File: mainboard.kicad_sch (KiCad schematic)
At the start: 95 parts, among them J1 Conn 02x05 1.27mm, J10 Micro_SD_Card, J2 TFM-110-12-L-D-A, J3 SFC-110-T2-F-D-A, J4 CLP-105-02-X-DH-A, J5 CLP-105-02-X-DH-A, J6 CLP-105-02-X-DH-A, J7 CLP-105-02-X-DH-A, J8 U.FL-R-SMT-1, J9 USB_C_Receptacle_USB2.0, SW1 KMR231NG, SW2 SW_SPDT, U1 ATSAMD51J20A-M, U10 USBLC6-2SC6, U11 PCF8523TK, U2 MAX706RESA+, U3 AP2112K-3.3, U4 MR25H40, U5 BMX160, U6 RFM98PW, U7 DRV8830DRC, U8 DRV8830DRC, U9 DRV8830DRC, Y1 32.768kHz, Y2 32.768kHz

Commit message: Added Pullup to SD CS
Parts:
- added R69: 10K, Resistor_SMD:R_0603_1608Metric, symbol Device:R_US
- R92, R93: symbol Device:R_Small -> Device:R_US
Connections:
- net +3V3: now also R69.1
- net SD_CS: now also R69.2
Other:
- note added: "I2C1 ADDR"
- note added: "I2C2 ADDR"
- note added: "X BOARD COILS I2C1 ADDR 0x60"
- note added: "Y BOARD COILS I2C1 ADDR 0x62"
- note added: "Z BOARD COILS I2C1 ADDR 0x68"
- note removed: "I2C ADDR"
- moved on the sheet: J4, J5, J6, J7, R26, R27, R28

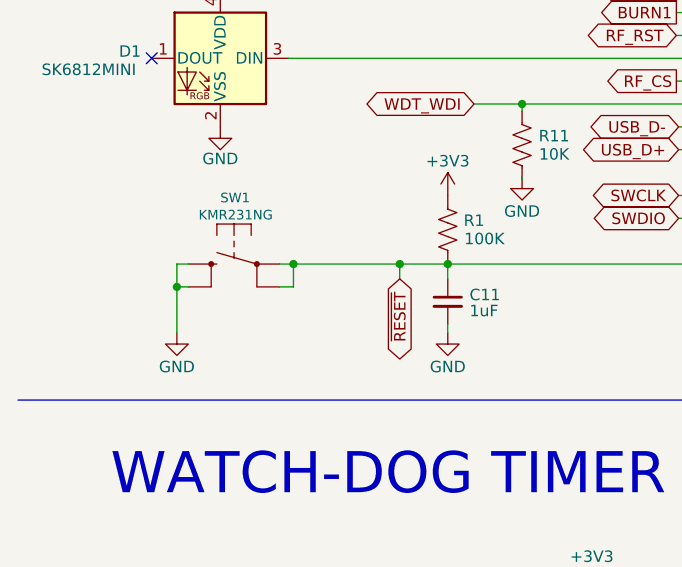
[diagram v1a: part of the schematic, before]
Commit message: right-angle reset button + export STEP / BOM
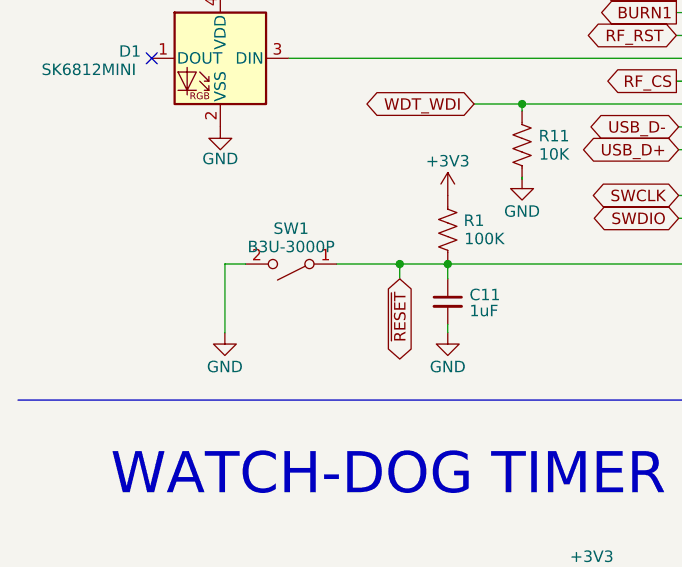
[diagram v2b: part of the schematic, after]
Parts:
- removed SW1: KMR231NG, mainboard:BTN_KMR2_4.6X2.8, symbol mainboard:SWITCH_TACT_SMT4.6X2.8-
- added SW1: B3U-3000P, Button_Switch_SMD:SW_SPST_B3U-3000P, symbol Switch:SW_SPST
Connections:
- net GND: now also SW1.2 (B)
- net ~{RESET}: now also SW1.1 (A)
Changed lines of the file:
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@@
   (junction (at 142.24 34.036) (diameter 0) (color 0 0 0 0)
   )
-  (junction (at 29.591 131.445) (diameter 0) (color 0 0 0 0)
-  )
   (junction (at 165.354 90.805) (diameter 0) (color 0 0 0 0)
   )
@@
   (junction (at 142.24 39.116) (diameter 0) (color 0 0 0 0)
   )
-  (junction (at 42.545 128.905) (diameter 0) (color 0 0 0 0)
-  )
   (junction (at 187.071 163.703) (diameter 0) (color 0 0 0 0)
   )
@@
     (stroke (width 0) (type default) (color 0 0 0 0))
   )
-  (wire (pts (xy 29.591 131.445) (xy 30.861 131.445))
-    (stroke (width 0) (type default) (color 0 0 0 0))
-  )
   (wire (pts (xy 386.588 189.357) (xy 393.065 189.357))
     (stroke (width 0) (type default) (color 0 0 0 0))
@@
     (stroke (width 0) (type default) (color 0 0 0 0))
   )
-  (wire (pts (xy 41.021 131.445) (xy 42.545 131.445))
-    (stroke (width 0) (type default) (color 0 0 0 0))
-  )
   (wire (pts (xy 182.372 38.1) (xy 178.816 38.1))
     (stroke (width 0) (type default) (color 0 0 0 0))
@@
     (stroke (width 0) (type default) (color 0 0 0 0))
   )
-  (wire (pts (xy 29.591 128.905) (xy 29.591 131.445))
-    (stroke (width 0) (type default) (color 0 0 0 0))
-  )
   (wire (pts (xy 142.367 83.185) (xy 142.367 85.725))
     (stroke (width 0) (type default) (color 0 0 0 0))
@@
     (stroke (width 0) (type default) (color 0 0 0 0))
   )
-  (wire (pts (xy 42.545 128.905) (xy 54.356 128.905))
+  (wire (pts (xy 47.371 128.905) (xy 54.356 128.905))
     (stroke (width 0) (type default) (color 0 0 0 0))
   )
@@
     (stroke (width 0) (type solid) (color 0 0 0 0))
   )
-  (wire (pts (xy 41.021 128.905) (xy 42.545 128.905))
-    (stroke (width 0) (type default) (color 0 0 0 0))
-  )
   (wire (pts (xy 342.138 213.741) (xy 343.789 213.741))
     (stroke (width 0) (type default) (color 0 0 0 0))
@@
     (stroke (width 0) (type default) (color 0 0 0 0))
   )
-  (wire (pts (xy 29.591 128.905) (xy 30.861 128.905))
+  (wire (pts (xy 34.925 128.905) (xy 37.211 128.905))
     (stroke (width 0) (type default) (color 0 0 0 0))
   )
@@
     (stroke (width 0) (type solid) (color 0 0 0 0))
   )
-  (wire (pts (xy 42.545 131.445) (xy 42.545 128.905))
-    (stroke (width 0) (type default) (color 0 0 0 0))
-  )
   (wire (pts (xy 247.142 145.542) (xy 247.142 148.082))
     (stroke (width 0) (type default) (color 0 0 0 0))
@@
     (stroke (width 0) (type default) (color 0 0 0 0))
   )
-  (wire (pts (xy 29.591 131.445) (xy 29.591 136.525))
+  (wire (pts (xy 34.925 128.905) (xy 34.925 136.525))
     (stroke (width 0) (type default) (color 0 0 0 0))
   )
@@
     )
   )
-  (symbol (lib_id "mainboard:SWITCH_TACT_SMT4.6X2.8-") (at 35.941 128.905 0) (mirror y) (unit 1)
-    (in_bom yes) (on_board yes)
-    (property "Reference" "SW1" (id 0) (at 37.719 122.174 0)
-      (effects (font (size 1.0668 1.0668)) (justify left bottom))
-    )
-    (property "Value" "KMR231NG" (id 1) (at 40.259 124.079 0)
-      (effects (font (size 1.0668 1.0668)) (justify left bottom))
-    )
-    (property "Footprint" "mainboard:BTN_KMR2_4.6X2.8" (id 2) (at 35.941 128.905 0)
-      (effects (font (size 1.27 1.27)) hide)
-    )
-    (property "Datasheet" "https://www.ckswitches.com/media/1479/kmr2.pdf" (id 3) (at 35.941 128.905 0)
-      (effects (font (size 1.27 1.27)) hide)
-    )
-    (pin "A")
-    (pin "A'")
-    (pin "B")
-    (pin "B'")
-  )
   (symbol (lib_id "Device:R_US") (at 59.69 125.095 180) (unit 1)
     (in_bom yes) (on_board yes)
@@
     (pin "1")
   )
-  (symbol (lib_id "power:GND") (at 29.591 136.525 0) (unit 1)
+  (symbol (lib_id "power:GND") (at 34.925 136.525 0) (unit 1)
     (in_bom yes) (on_board yes)
-    (property "Reference" "#PWR02" (id 0) (at 29.591 142.875 0)
+    (property "Reference" "#PWR02" (id 0) (at 34.925 142.875 0)
       (effects (font (size 1.27 1.27)) hide)
     )
-    (property "Value" "GND" (id 1) (at 29.591 140.335 0))
-    (property "Footprint" "" (id 2) (at 29.591 136.525 0)
+    (property "Value" "GND" (id 1) (at 34.925 140.335 0))
+    (property "Footprint" "" (id 2) (at 34.925 136.525 0)
       (effects (font (size 1.27 1.27)) hide)
     )
-    (property "Datasheet" "" (id 3) (at 29.591 136.525 0)
+    (property "Datasheet" "" (id 3) (at 34.925 136.525 0)
       (effects (font (size 1.27 1.27)) hide)
     )
@@
     (pin "1")
   )
+  (symbol (lib_id "Switch:SW_SPST") (at 42.291 128.905 180) (unit 1)
+    (in_bom yes) (on_board yes)
+    (property "Reference" "SW1" (id 0) (at 42.291 124.968 0))
+    (property "Value" "B3U-3000P" (id 1) (at 42.291 127 0))
+    (property "Footprint" "Button_Switch_SMD:SW_SPST_B3U-3000P" (id 2) (at 42.291 128.905 0)
+      (effects (font (size 1.27 1.27)) hide)
+    )
+    (property "Datasheet" "~" (id 3) (at 42.291 128.905 0)
+      (effects (font (size 1.27 1.27)) hide)
+    )
+    (pin "1")
+    (pin "2")
+  )
   (symbol (lib_id "Device:R_US") (at 359.283 38.735 90) (unit 1)
     (in_bom yes) (on_board yes)
@@
       (reference "R106") (unit 1) (value "10K") (footprint "Resistor_SMD:R_0603_1608Metric")
     )
-    (path "/00000000-0000-0000-0000-00005c6b86a4"
-      (reference "SW1") (unit 1) (value "KMR231NG") (footprint "mainboard:BTN_KMR2_4.6X2.8")
+    (path "/ace5ed3d-6dc5-4eeb-9b9e-b9cae91d4881"
+      (reference "SW1") (unit 1) (value "B3U-3000P") (footprint "Button_Switch_SMD:SW_SPST_B3U-3000P")
     )
     (path "/b6f24720-0eec-4e84-ad7b-6ef73d6ff170"

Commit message: Cleanup
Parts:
- C6: renamed from C7; value 10pF -> 4pF
- C7: renamed from C6; value 10pF -> 4pF
- D1: value SK6812MINI -> SK6812-MINI; footprint mainboard:NeoPixel 3535 -> LED_SMD:LED_SK6812MINI_PLCC4_3.5x3.5mm_P1.75mm
- J2: renamed from J8; symbol mainboard:U.FL-R-SMT-1-symbols -> mainboard:U.FL-R-SMT-1
- J5: renamed from J3; value SFC-110-T2-F-D-A -> SFC-110-T2-X-D-A
- J6: renamed from J2; value TFM-110-12-L-D-A -> TFM-110-12-X-D-A
- U1: value ATSAMD51J20A-M -> ATSAMD51J19A-M; symbol mainboard:ATSAMD51J20A-M-MCU_Microchip_SAMD -> mainboard:ATSAMD51J19A-M
- U2: symbol mainboard:MAX708RESA-T-symbols -> mainboard:MAX708RESA-T
- U5: symbol mainboard:BMX160-symbols -> mainboard:BMX160
- U6: symbol mainboard:RFM98PW-symbols -> mainboard:RFM98PW
- U7, U8, U9: symbol mainboard:DRV8830DRC-wbraun_ic_lib -> mainboard:DRV8830DRC
- renumbered C34 to C12, C12 to C13, C13 to C14, C14 to C15, C15 to C16, C32 to C17, C33 to C18, C16 to C19, C18 to C20, C19 to C21, C35 to C22, C20 to C23, C21 to C24, C22 to C25, C23 to C26, C17 to C27, J7 to J10, J10 to J3, J9 to J4, J4 to J7, J5 to J8, J6 to J9, R3 to R1, R11 to R10, R1 to R11, R22 to R12, R12 to R13, R13 to R14, R80 to R15, R14 to R16, R15 to R17, R16 to R18, R69 to R19, R4 to R2, R18 to R20, R19 to R21, R20 to R22, R17 to R26, R70 to R27, R93 to R28, R92 to R29, R9 to R3, R26 to R30, R27 to R31, R28 to R32, R10 to R4, R21 to R9
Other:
- note added: "Check Xtal Datasheet This value assumes 7pF crystal bulk capacitance"
- note added: "RTC supports 7pF (default) and 12.5pF crystal capacitance only"
- moved on the sheet: C13, C19

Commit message: Stash before major changes
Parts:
- removed SW1: B3U-3000P, Button_Switch_SMD:SW_SPST_B3U-3000P, symbol Switch:SW_SPST
- added Q23: IRLML2803, Package_TO_SOT_SMD:SOT-23, symbol Transistor_FET:IRLML2060
- added R103: DNI (0R), Resistor_SMD:R_0603_1608Metric, symbol Device:R_US
- added R104: 200K, Resistor_SMD:R_0603_1608Metric, symbol Device:R_US
- added SW1: KMS233, mainboard:BTN_KMS2, symbol mainboard:BTN_KMS2
- D1: footprint LED_SMD:LED_SK6812MINI_PLCC4_3.5x3.5mm_P1.75mm -> mainboard:SK6812-MINI
- J3: footprint mainboard:microSD_HC_Molex_104031-0811 -> mainboard:microSD_104031-0811; symbol Connector:Micro_SD_Card_Det -> Connector:Micro_SD_Card_Det2
- J5: footprint mainboard:SAMTEC_SFC-110-T2-F-D-A-TR -> mainboard:SAMTEC_SFC-110-T2-X-D-A
- J6: footprint mainboard:SAMTEC_TFM-110-12-L-D-A -> mainboard:SAMTEC_TFM-110-12-X-D-A
- R20, R21, R22, R26, R30, R31, R32: value 0 -> 0R
- R28, R29: value 22 -> 22R
- SW2: value SW_SPDT -> PCM12SMTR; footprint mainboard:SW_PCM12SMTR -> mainboard:PCM12SMTR
- U2: symbol mainboard:MAX708RESA-T -> mainboard:MAX708RESA+
- U4: footprint mainboard:SON127P600X500X90-9N -> mainboard:MR25H40DF
- U6: footprint mainboard:RFM95PW -> mainboard:RFM98PW
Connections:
- net GND: now also R104.2, SW1.1 (S), SW1.2 (S1), SW1.5
- net ~{RESET}: now also Q23.3 (D), R103.1, SW1.3 (P), SW1.4 (P1); no longer R13.1
- net WDT_EN: now reaches U1.49 (PB22)
- net WDT_EN: now also Q23.1 (G), R104.1
- new net: Q23.2 (S), R103.2, R13.1
- no-connect marks 35 -> 34
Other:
- note added: "WDT able to reset MCU when WDT_EN is high"
- note removed: "WDT enabled when installed"
- moved on the sheet: C13, R11, R13, U2

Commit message: Finished routing Rev B3/01
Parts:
- removed D1: SK6812-MINI, mainboard:SK6812-MINI, symbol LED:SK6812MINI
- removed FID1, FID2, FID3: Fiducial, Fiducial:Fiducial_0.5mm_Mask1mm, symbol Mechanical:Fiducial
- removed SW2: PCM12SMTR, mainboard:PCM12SMTR, symbol Switch:SW_SPDT
- removed U5: BMX160, mainboard:BMX160, symbol mainboard:BMX160
- added C36: 0.1uF, Capacitor_SMD:C_0603_1608Metric, symbol Device:C_Small
- added C37, C38: 22pF, Capacitor_SMD:C_0603_1608Metric, symbol Device:C_Small
- added D1: SK6812-SIDE, mainboard:SK6812-SIDE, symbol mainboard:SK6812-SIDE
- added D2: MBR1020VL-AU_R1, Diode_SMD:D_SOD-123F, symbol Device:D_Schottky_Small
- added Q20: SQ3495EV-T1, Package_TO_SOT_SMD:SOT-23-6, symbol cameraboard:SQ3495EV-T1
- added R81, R82, R83: 10K, Resistor_SMD:R_0603_1608Metric, symbol Device:R_US
- added U12: BNO085, mainboard:BNO085, symbol mainboard:BNO085
- added U5: LTC4412xS6, Package_TO_SOT_SMD:TSOT-23-6, symbol Power_Management:LTC4412xS6
- added Y3: 32.768kHz, Crystal:Crystal_SMD_MicroCrystal_CC7V-T1A-2Pin_3.2x1.5mm, symbol Device:Crystal_Small
- C20: value 0.1uF -> 1uF
- renumbered Q23 to Q21, R104 to R100, R103 to R99
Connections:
- net +3V3: now also R18.2, D1.2 (VDD), R81.2, R82.1, U12.28 (VDDIO), U12.3 (VDD), U12.5 (PS1), U12.6 (PS0/WAKE); no longer C20.1, R18.1
- net BATT_P: now also C20.1, Q20.1 (D), Q20.2 (D), Q20.5 (D), Q20.6 (D), U5.1 (VIN)
- net GND: now also C36.2, C37.1, C38.2, D1.4 (VSS), R83.1, U12.10 (CLKSEL0), U12.2 (GND), U12.25 (GNDIO), U5.2 (GND), U5.3 (CTL)
- net HI_POW: now also D2.1 (K), Q20.4 (S), U5.6 (SENSE); no longer U8.7 (A0), U8.8 (A1), U9.7 (A0)
- net VUSB_IN: now also D2.2 (A)
- net IMU_CS: now reaches U1.32 (PA15)
- net IMU_CS: now also R82.2, U12.18 (H_CSN)
- net at U1.42 (PA21): now also D1.1 (DIN)
- new net: C37.2, U12.27 (XIN32), Y3.1
- new net: C38.1, U12.26 (CLKSEL1/XOUT32), Y3.2
- new net: C36.1, U12.9 (CAP)
- new net: Q20.3 (G), U5.5 (GATE)
- new net: R81.1, U12.11 (NRST)
- new net: R18.1, U12.4 (BOOTN)
- new net: U12.1 (NC), U12.12 (NC), U12.13 (NC), U12.21 (NC), U12.22 (NC), U12.23 (NC), U12.24 (NC), U12.7 (NC), U12.8 (NC)
- new net ADPT_STAT: U5.4 (STAT)
- new net IMU_MISO: U12.20 (H_SDA/MISO/TX)
- new net IMU_MOSI: R83.2, U12.17 (H_SA0/MOSI)
- new net IMU_SCK: U12.19 (H_SCL/SCLK/RX)
- no-connect marks 34 -> 35
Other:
- note added: "Coil Driver Circuits"
- note added: "HI-POW SELECT"
- note added: "IMU datasheet recommends 12.5pF crystal capacitance"
- note added: "Y BOARD COILS I2C1 ADDR 0x61"
- note added: "Z BOARD COILS I2C1 ADDR 0x64"
- note removed: "0x69"
- note removed: "I2C1 ADDR"
- note removed: "Right angle connectors"
- note removed: "Y BOARD COILS I2C1 ADDR 0x62"
- note removed: "Z BOARD COILS I2C1 ADDR 0x68"
- moved on the sheet: C1, C10, C11, C12, C13, C14, C15, C16, C17, C18, C19, C2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

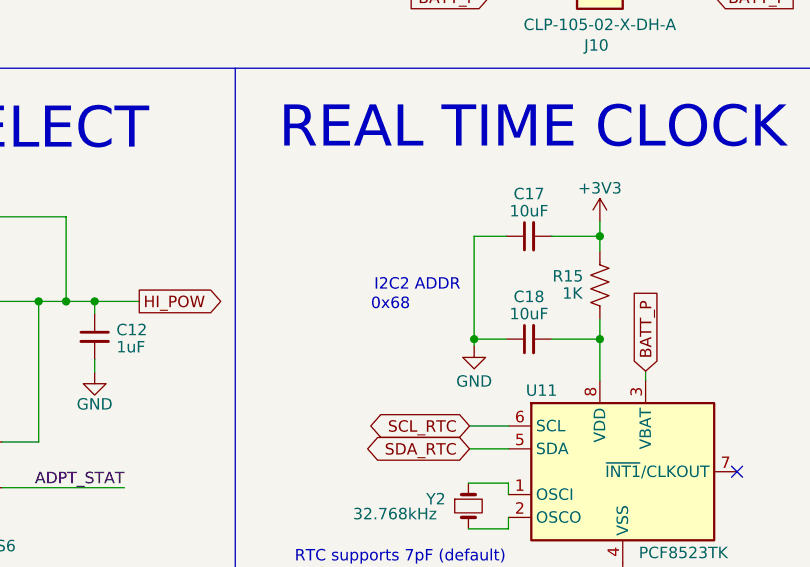
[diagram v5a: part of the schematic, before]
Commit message: Updated Schematic to reflect RTC on I2C 1
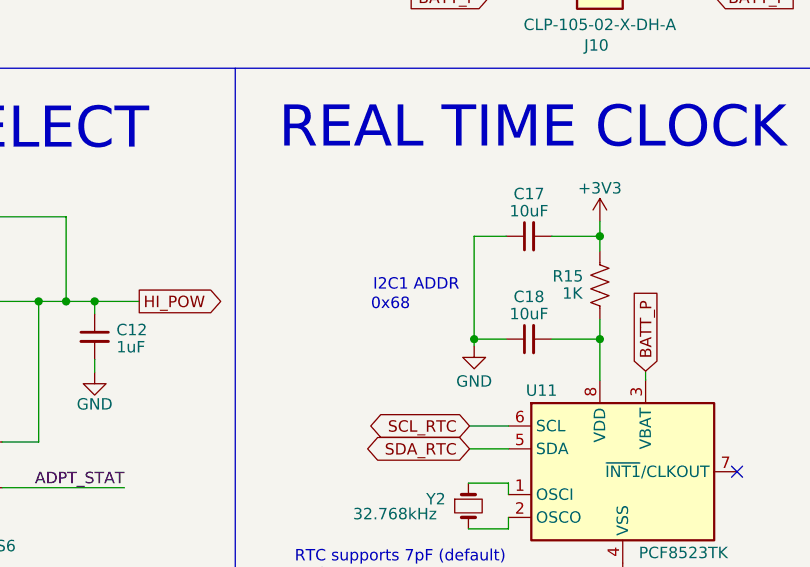
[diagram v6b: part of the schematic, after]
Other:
- note added: "I2C1 ADDR"
- note removed: "I2C2 ADDR"
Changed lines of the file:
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@@
     (effects (font (size 1.27 1.27)) (justify left bottom))
   )
-  (text "I2C2 ADDR" (at 176.784 168.91 0)
+  (text "I2C1 ADDR" (at 176.657 168.91 0)
     (effects (font (size 1.27 1.27)) (justify right bottom))
   )

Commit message: Rev B3/02 Updates
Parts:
- FL1, FL2, FL3: value EMI_Filter_CommonMode -> SRF2012
- H1, H2, H3, H4: now left out of the parts list
- R13: value 3.3K -> 0R
- SW1: value KMS233 -> 434331045822; footprint mainboard:BTN_KMS2 -> mainboard:SMT_1045822_WRE; symbol mainboard:BTN_KMS2 -> mainboard:BTN_434331045822
- Y1, Y2: value 32.768kHz -> 32.768kHz/7pF
- Y3: value 32.768kHz -> 32.768kHz/12.5pF
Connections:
- net GND: now also SW1.3 (P1); no longer SW1.2 (S1), SW1.5
- net PAYLOAD_EN: now also U1.12 (PB09); no longer U1.39 (PB16)
- net ~{RESET}: now also SW1.2 (S); no longer SW1.3 (P)
- net IMU_RST: now reaches U1.40 (PB17)
- net IMU_RST: now also R81.1, U12.11 (NRST)
- net IMU_INT: now reaches U12.14 (H_INTN)
- net IMU_INT: now also U1.39 (PB16)
- no-connect marks 35 -> 32
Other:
- moved on the sheet: C37, C38, C6, C7, R81, Y1, Y3
